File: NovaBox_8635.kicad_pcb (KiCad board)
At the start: 2 copper layers, 82 x 30 mm, 87 parts, among them P1 MH, P2 MH, P3 MH, P4 MH, P5 USB, Q1 MMBT3904, Q2 IRLML6344, Q3 IRLML6401, Q4 MMBT3904, Q5 MMBT3904, SW1 PIO18, SW2 PIO21, SW3 PIO8, SW4 PIO0, SW5 PIO1, SW6 ON/OFF, U1 MCP6004, U2 CSR8635_MODULE, U3 CSR_DebugSmall, U4 PAM8304, U5 PAM8304, U6 LT1308

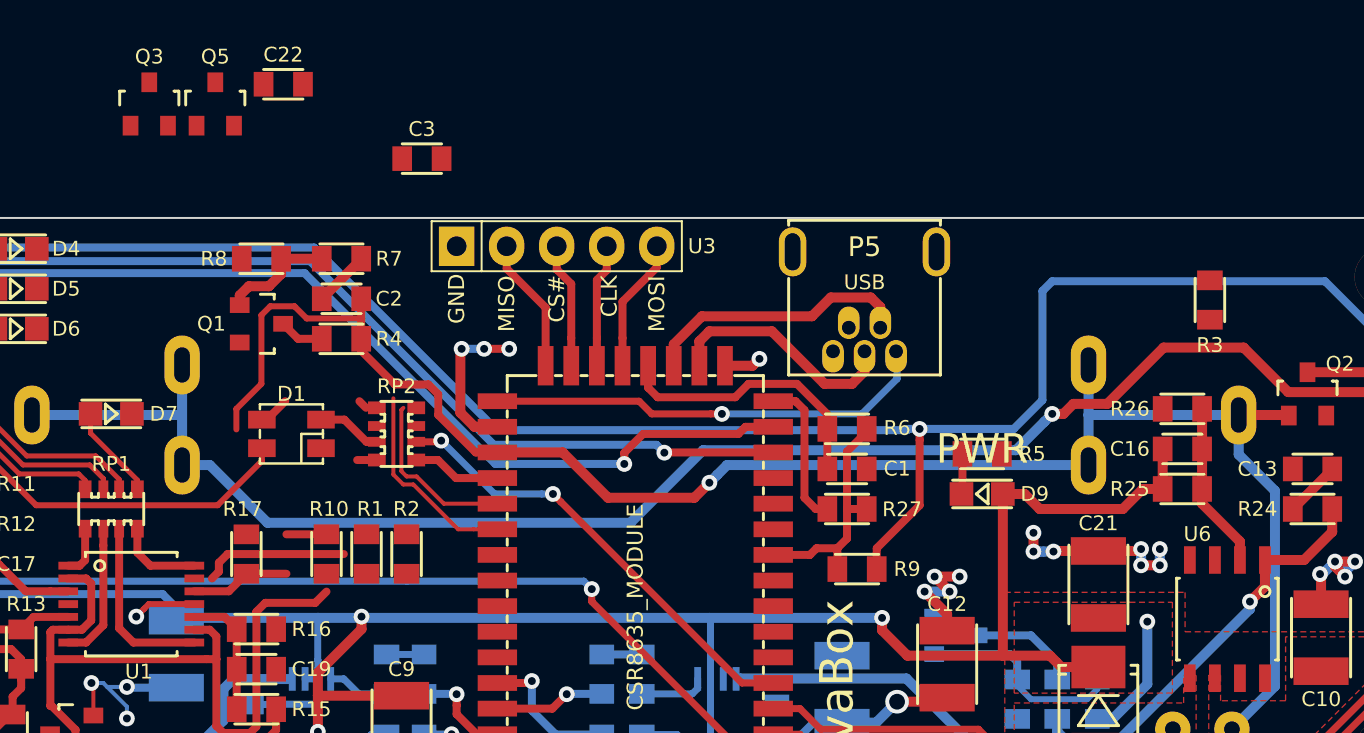
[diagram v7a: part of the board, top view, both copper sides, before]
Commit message: moved new components around; showing pin names on PMOS and NMOS
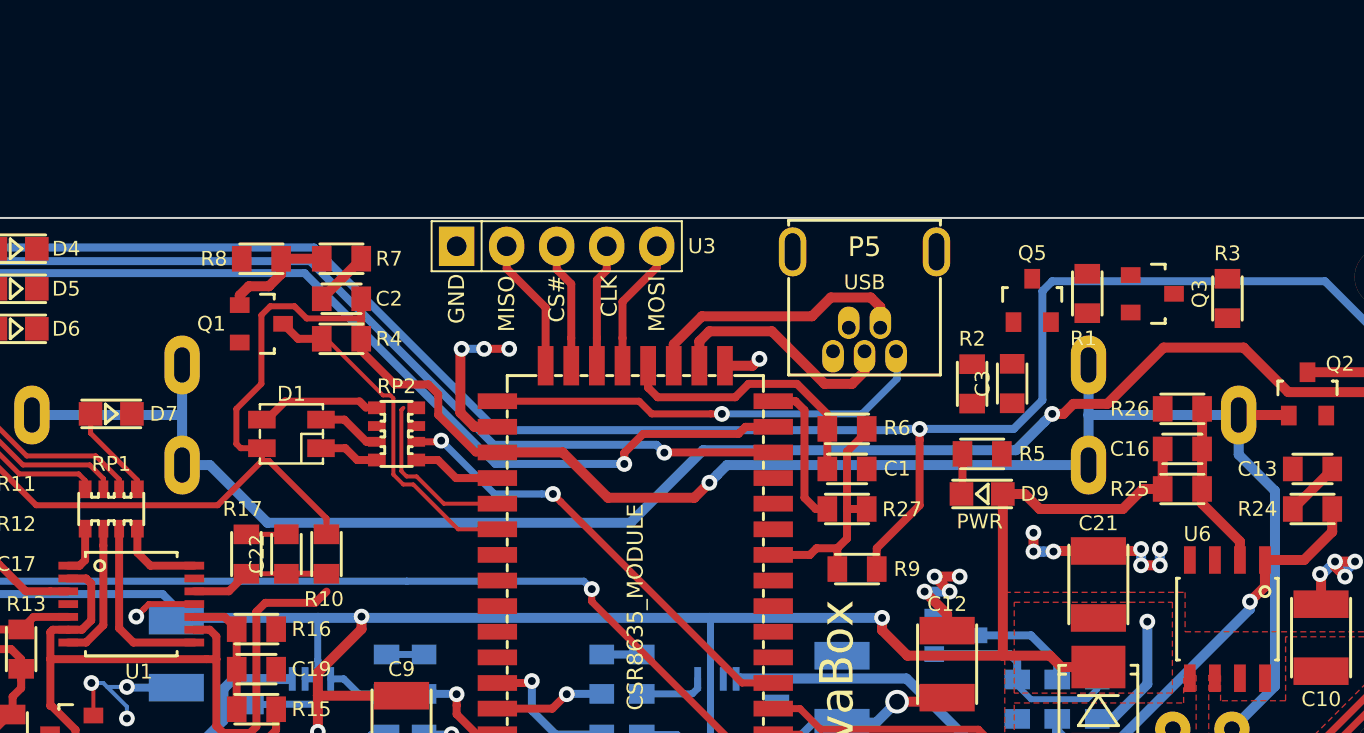
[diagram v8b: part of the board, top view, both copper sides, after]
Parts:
- moved Q3 51.8 mm to (126.2, 53.8), turned to 270 degrees
- moved Q5 42.6 mm to (120.1, 54.2)
- moved R1 38.9 mm to (122.9, 53.8), turned to 90 degrees
- moved C3 32.1 mm to (119.1, 58.4), turned to 90 degrees
- moved R2 30.0 mm to (117.1, 58.4)
- moved C22 23.8 mm to (82.3, 67.1), turned to 90 degrees
- moved R3 0.89 mm to (130.0, 54.1), turned to 270 degrees
- turned R10 to 90 degrees
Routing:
- net +BATT: track 153.0 -> 161.0 mm
- net Net-(R1-Pad1): track 7.47 -> 0.00 mm
- net PWER_E: track 12.7 -> 17.5 mm
- net Net-(D1-Pad3): track 2.05 -> 5.81 mm
- net Net-(D1-Pad1): track 1.00 -> 3.08 mm
- net GND: track 50.9 -> 52.9 mm
- net Net-(C22-Pad1): track 7.62 -> 7.07 mm
